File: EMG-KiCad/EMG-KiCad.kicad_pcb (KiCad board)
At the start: 2 copper layers, 44 parts, among them J1 Conn_01x03_Socket, J3 Conn_01x02_Socket, J4 Conn_01x01_Socket, U0 AD623, U1 OPA2333xxD, U2 OPA2333xxD, U3 OPA333xxDBV, U4 OPA350UA, U5 LDO 3.3, U6 LDO 1.5

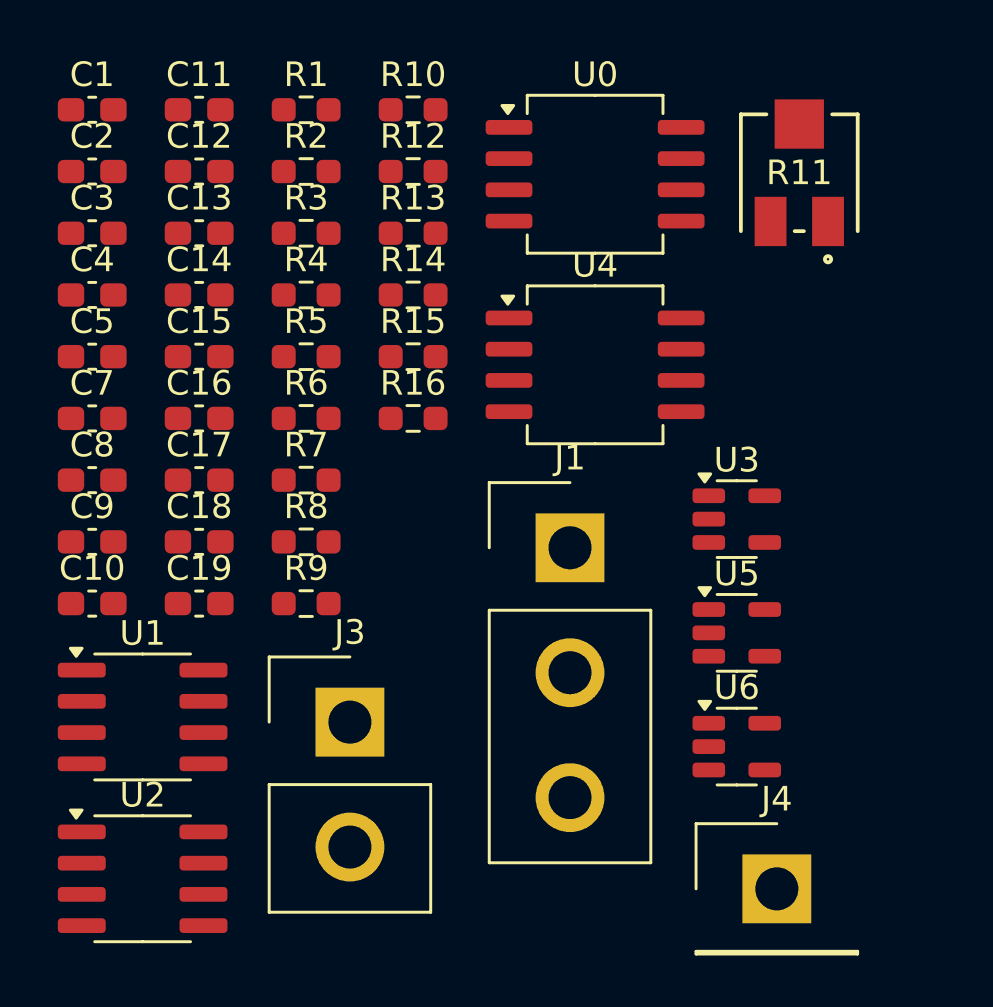
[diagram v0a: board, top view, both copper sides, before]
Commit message: complete the pcb traces
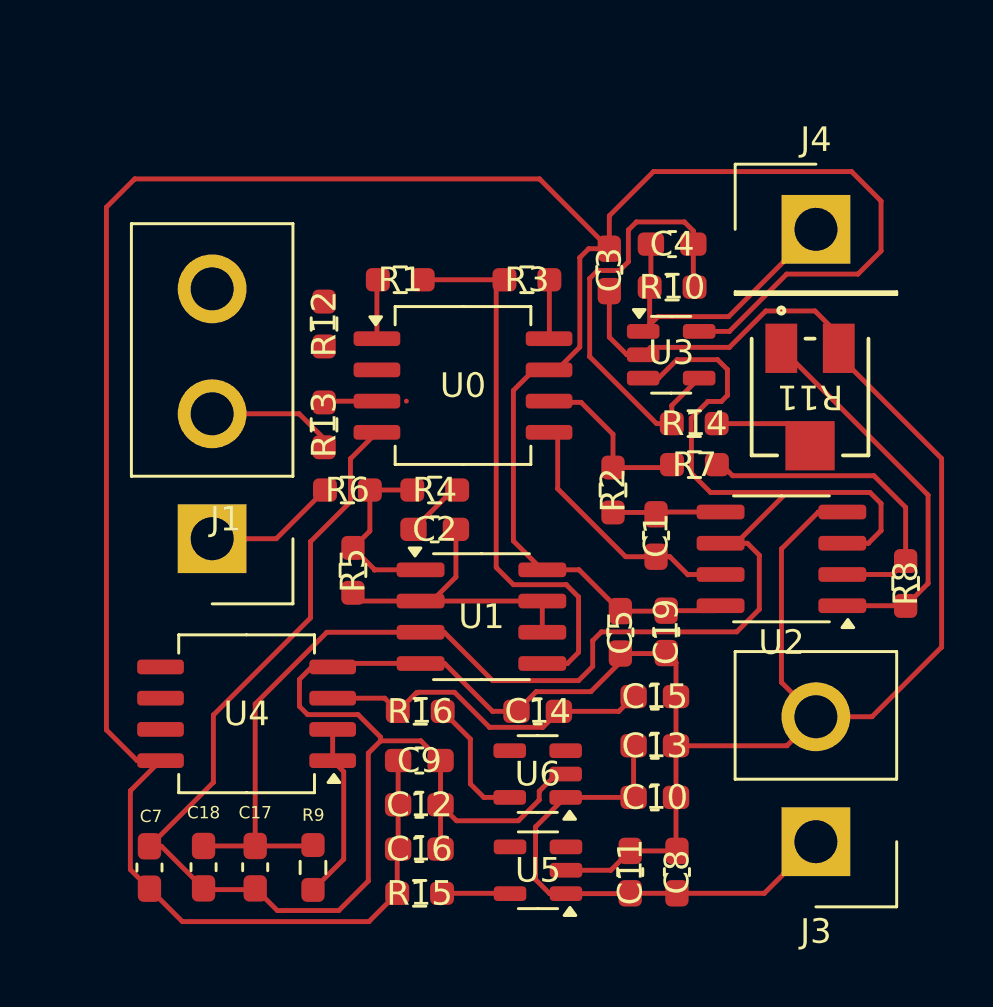
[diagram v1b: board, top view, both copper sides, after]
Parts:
- moved C11 35.6 mm to (154.5, 110.8), turned to 90 degrees
- moved U2 29.1 mm to (160.7, 98.1), turned to 180 degrees
- moved C1 28.7 mm to (155.6, 97.1), turned to 90 degrees
- moved C8 28.6 mm to (156.4, 110.8), turned to 90 degrees
- moved C13 27.9 mm to (155.5, 105.7)
- moved C12 27.3 mm to (146.0, 108.1)
- moved J4 26.9 mm to (162.1, 84.7)
- moved R8 24.4 mm to (165.7, 99.1), turned to 90 degrees
- moved C5 24.2 mm to (154.1, 101.1), turned to -90 degrees
- moved C10 24.2 mm to (155.5, 107.8)
- moved C4 23.7 mm to (156.2, 85.3), turned to 180 degrees
- moved C15 23.1 mm to (155.5, 103.7)
- moved R15 21.8 mm to (146.0, 111.7), turned to 180 degrees
- moved C14 21.8 mm to (150.8, 104.3), turned to 180 degrees
- moved C3 21.1 mm to (153.7, 86.3), turned to 90 degrees
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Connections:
- R12 pad 1: Net-(J1-Pin_2) -> Net-(J1-Pin_3)
- R13 pad 1: Net-(J1-Pin_3) -> Net-(J1-Pin_2)
- U0 pad 4: /V- -> Earth
- U3 pad 2: unconnected-(U3-V--Pad2) -> Earth
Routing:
- net Earth: track 0.00 -> 135.4 mm
- net /V+: track 0.00 -> 117.4 mm
- net /Vref: track 0.00 -> 63.2 mm
- net Net-(U1B-+): track 0.00 -> 22.9 mm
- net /Vpower: track 0.00 -> 22.6 mm
- net Net-(U3--): track 0.00 -> 18.3 mm
- net Net-(R11-Pad1): track 0.00 -> 15.9 mm
- net Net-(U4A-+): track 0.00 -> 13.9 mm
- net Net-(U2A--): track 0.00 -> 13.4 mm
- net Net-(U1A--): track 0.00 -> 12.9 mm
- net /Vout: track 0.00 -> 12.4 mm
- net Net-(U0-Ref): track 0.00 -> 10.3 mm
- net Net-(R4-Pad1): track 0.00 -> 7.50 mm
- net Net-(U4A--): track 0.00 -> 7.23 mm
- net Net-(R2-Pad2): track 0.00 -> 6.59 mm
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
